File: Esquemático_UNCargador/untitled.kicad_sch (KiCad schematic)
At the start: 14 parts, among them U3.3 LM2596S-3.3, U5 LM2596S-5

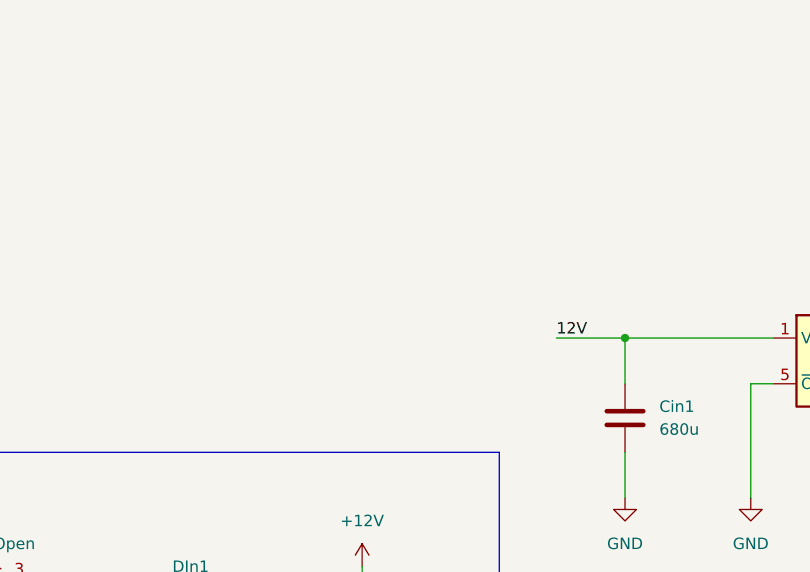
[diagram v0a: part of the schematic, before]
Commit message: Se modifica esquema del micro y se agrega página de sensores
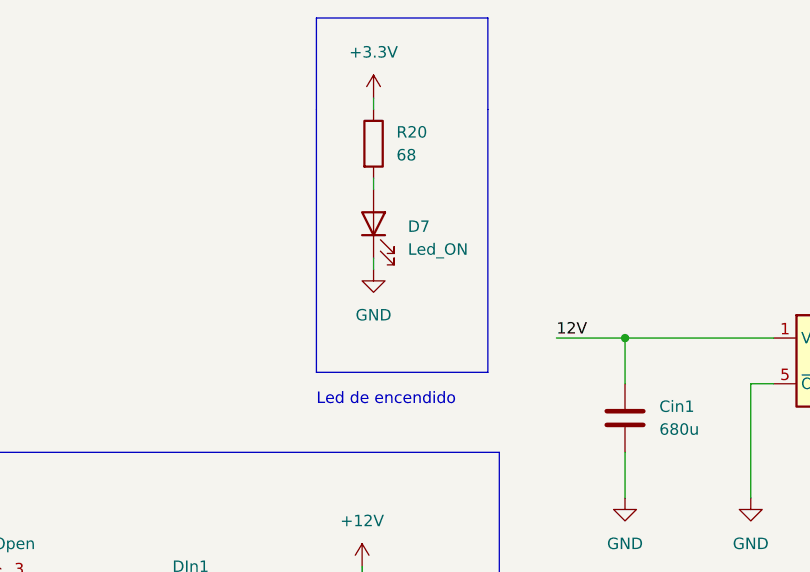
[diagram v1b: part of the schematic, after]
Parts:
- added D7: Led_ON, LED_SMD:LED_0603_1608Metric_Pad1.05x0.95mm_HandSolder, symbol LED:IR26-21C_L110_TR8
- added R20: 68, Resistor_SMD:R_1206_3216Metric_Pad1.30x1.75mm_HandSolder, symbol Device:R
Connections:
- net +3.3V: now also R20.1
- net GND: now also D7.1 (K)
- new net: D7.2 (A), R20.2
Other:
- note added: "Led de encendido"
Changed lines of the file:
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@@
+    (stroke (width 0) (type default))
+  )
+  (polyline (pts (xy 156.21 33.02) (xy 156.21 22.86))
+    (stroke (width 0) (type default))
+  )
+  (polyline (pts (xy 156.21 22.86) (xy 175.26 22.86))
+    (stroke (width 0) (type default))
+  )
+  (polyline (pts (xy 175.26 62.23) (xy 175.26 33.02))
+    (stroke (width 0) (type default))
+  )
+  (wire (pts (xy 162.56 31.75) (xy 162.56 33.02))
     (stroke (width 0) (type default))
   )
@@
     (stroke (width 0) (type default))
   )
+  (wire (pts (xy 162.56 49.53) (xy 162.56 50.8))
+    (stroke (width 0) (type default))
+  )
   (wire (pts (xy 161.29 90.17) (xy 168.91 90.17))
     (stroke (width 0) (type default))
@@
     (stroke (width 0) (type default))
   )
+  (polyline (pts (xy 156.21 33.02) (xy 156.21 62.23))
+    (stroke (width 0) (type default))
+  )
   (wire (pts (xy 219.71 120.65) (xy 219.71 128.27))
     (stroke (width 0) (type default))
@@
     (stroke (width 0) (type default))
   )
+  (wire (pts (xy 162.56 40.64) (xy 162.56 41.91))
+    (stroke (width 0) (type default))
+  )
   (wire (pts (xy 190.5 71.12) (xy 190.5 76.2))
     (stroke (width 0) (type default))
@@
   )
   (wire (pts (xy 232.41 63.5) (xy 237.49 63.5))
+    (stroke (width 0) (type default))
+  )
+  (polyline (pts (xy 175.26 22.86) (xy 175.26 33.02))
+    (stroke (width 0) (type default))
+  )
+  (polyline (pts (xy 156.21 62.23) (xy 175.26 62.23))
     (stroke (width 0) (type default))
   )
@@
     (effects (font (size 1.27 1.27)) (justify left bottom))
   )
+  (text "Led de encendido\n" (at 156.21 66.04 0)
+    (effects (font (size 1.27 1.27)) (justify left bottom))
+  )
   (label "12V" (at 182.88 110.49 0) (fields_autoplaced)
     (effects (font (size 1.27 1.27)) (justify left bottom))
@@
     )
   )
+  (symbol (lib_id "Device:R") (at 162.56 36.83 0) (unit 1)
+    (in_bom yes) (on_board yes) (dnp no) (fields_autoplaced)
+    (property "Reference" "R20" (at 165.1 35.5599 0)
+      (effects (font (size 1.27 1.27)) (justify left))
+    )
+    (property "Value" "68" (at 165.1 38.0999 0)
+      (effects (font (size 1.27 1.27)) (justify left))
+    )
+    (property "Footprint" "Resistor_SMD:R_1206_3216Metric_Pad1.30x1.75mm_HandSolder" (at 160.782 36.83 90)
+      (effects (font (size 1.27 1.27)) hide)
+    )
+    (property "Datasheet" "~" (at 162.56 36.83 0)
+      (effects (font (size 1.27 1.27)) hide)
+    )
+    (pin "1")
+    (pin "2")
+    (instances
+      (project "CircuitoPotencia"
+        (path "/f64e4c48-29c2-4644-b6e3-d55b9152fc29/c38372d7-094a-4ec0-82ac-c3a161d378bf"
+          (reference "R20") (unit 1)
+        )
+      )
+    )
+  )
   (symbol (lib_id "power:GND") (at 259.08 128.27 0) (unit 1)
     (in_bom yes) (on_board yes) (dnp no) (fields_autoplaced)
@@
         (path "/f64e4c48-29c2-4644-b6e3-d55b9152fc29/c38372d7-094a-4ec0-82ac-c3a161d378bf"
           (reference "COut1") (unit 1)
+        )
+      )
+    )
+  )
+  (symbol (lib_id "power:GND") (at 162.56 50.8 0) (unit 1)
+    (in_bom yes) (on_board yes) (dnp no) (fields_autoplaced)
+    (property "Reference" "#PWR032" (at 162.56 57.15 0)
+      (effects (font (size 1.27 1.27)) hide)
+    )
+    (property "Value" "GND" (at 162.56 55.88 0)
+      (effects (font (size 1.27 1.27)))
+    )
+    (property "Footprint" "" (at 162.56 50.8 0)
+      (effects (font (size 1.27 1.27)) hide)
+    )
+    (property "Datasheet" "" (at 162.56 50.8 0)
+      (effects (font (size 1.27 1.27)) hide)
+    )
+    (pin "1")
+    (instances
+      (project "CircuitoPotencia"
+        (path "/f64e4c48-29c2-4644-b6e3-d55b9152fc29/c38372d7-094a-4ec0-82ac-c3a161d378bf"
+          (reference "#PWR032") (unit 1)
         )
       )
@@
     )
   )
+  (symbol (lib_id "LED:IR26-21C_L110_TR8") (at 162.56 45.72 90) (unit 1)
+    (in_bom yes) (on_board yes) (dnp no) (fields_autoplaced)
+    (property "Reference" "D7" (at 166.37 46.0374 90)
+      (effects (font (size 1.27 1.27)) (justify right))
+    )
+    (property "Value" "Led_ON" (at 166.37 48.5774 90)
+      (effects (font (size 1.27 1.27)) (justify right))
+    )
+    (property "Footprint" "LED_SMD:LED_0603_1608Metric_Pad1.05x0.95mm_HandSolder" (at 157.48 45.72 0)
+      (effects (font (size 1.27 1.27)) hide)
+    )
+    (property "Datasheet" "http://www.everlight.com/file/ProductFile/IR26-21C-L110-TR8.pdf" (at 162.56 45.72 0)
+      (effects (font (size 1.27 1.27)) hide)
+    )
+    (pin "1")
+    (pin "2")
+    (instances
+      (project "CircuitoPotencia"
+        (path "/f64e4c48-29c2-4644-b6e3-d55b9152fc29/c38372d7-094a-4ec0-82ac-c3a161d378bf"
+          (reference "D7") (unit 1)
+        )
+      )
+    )
+  )
   (symbol (lib_id "power:GND") (at 161.29 109.22 0) (unit 1)
     (in_bom yes) (on_board yes) (dnp no) (fields_autoplaced)
@@
         )
       )
+    )
+  )
+  (symbol (lib_id "power:+3.3V") (at 162.56 31.75 0) (unit 1)
+    (in_bom yes) (on_board yes) (dnp no) (fields_autoplaced)
+    (property "Reference" "#PWR031" (at 162.56 35.56 0)
+      (effects (font (size 1.27 1.27)) hide)
+    )
+    (property "Value" "+3.3V" (at 162.56 26.67 0)
+      (effects (font (size 1.27 1.27)))
+    )
+    (property "Footprint" "" (at 162.56 31.75 0)
+      (effects (font (size 1.27 1.27)) hide)
+    )
+    (property "Datasheet" "" (at 162.56 31.75 0)
+      (effects (font (size 1.27 1.27)) hide)
+    )
+    (pin "1")
+    (instances
+      (project "CircuitoPotencia"
+        (path "/f64e4c48-29c2-4644-b6e3-d55b9152fc29/c38372d7-094a-4ec0-82ac-c3a161d378bf"
+          (reference "#PWR031") (unit 1)
+        )
+      )

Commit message: Pinout sensores
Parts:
- removed D7: Led_ON, LED_SMD:LED_0603_1608Metric_Pad1.05x0.95mm_HandSolder, symbol LED:IR26-21C_L110_TR8
- removed PS7: HLK-PM01, Convertidor_AC-DC:AC-DC_Converter, symbol Converter_ACDC:HLK-PM01
- removed R20: 68, Resistor_SMD:R_1206_3216Metric_Pad1.30x1.75mm_HandSolder, symbol Device:R
- added CIn? (x2): ~, symbol Device:C
- added U?: ~, symbol Regulator_Linear:LM7912_TO220
- CIn0: value 22uF -> ~; footprint Capacitor_SMD:C_0805_2012Metric_Pad1.18x1.45mm_HandSolder -> (none)
- CIn2: value 680u -> ~; footprint Capacitor_SMD:C_0201_0603Metric -> (none)
- COut1, COut2: value 220u -> ~; footprint Capacitor_SMD:C_0201_0603Metric -> (none)
- Cin1: value 680u -> ~; footprint Capacitor_SMD:C_0805_2012Metric_Pad1.18x1.45mm_HandSolder -> (none)
- D1, D2: value 1N5822 -> ~; footprint Diode_THT:D_DO-201AD_P15.24mm_Horizontal -> (none)
- DIn: renamed from DIn1; value 1N4007 -> ~; footprint Diode_SMD:D_SMA_Handsoldering -> (none)
- JP?: renamed from JP2; value Jumper_3_Open -> ~; footprint Connector_PinHeader_2.54mm:PinHeader_1x03_P2.54mm_Vertical -> (none)
- L1, L2: value 33u -> ~; footprint Inductor_SMD:L_Coilcraft_XxL4040 -> (none)
- U3.3: value LM2596S-3.3 -> ~; footprint Package_TO_SOT_SMD:TO-263-5_TabPin3 -> (none)
- U5: value LM2596S-5 -> ~; footprint Package_TO_SOT_SMD:TO-263-5_TabPin3 -> (none)
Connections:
- net GND: now also CIn?.1, CIn?.1, U?.1 (GND)
- new net: CIn?.2, U?.3 (VO)
- new net: CIn?.2, U?.2 (VI)
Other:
- note removed: "Led de encendido"
- moved on the sheet: CIn0, CIn2, COut1, COut2, Cin1, D1, D2, DIn, JP?, L1, L2, U3.3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

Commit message: Actualización11/04/2023
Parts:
- added PS1: BAC05S05DC, ConvertidorAc-DC-Footprint-Loca:AC-DC_ConverterEditado, symbol Converter_ACDC:BAC05S05DC
- CIn2, Cin1: value ~ -> 680u
- COut1, COut2: value ~ -> 220u
- L1, L2: value ~ -> 33u
- gave numbers to parts that had none: 1
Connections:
- net GND: now also PS1.4 (-Vo)
- net at JP1.2 (C): now also PS1.5 (+Vo)
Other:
- moved on the sheet: CIn0, CIn2, CIn?, COut1, COut2, Cin1, D1, D2, DIn, JP1, L1, L2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

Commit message: Actualización_huellas_Potencia
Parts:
- CIn0: value ~ -> 22mF; footprint (none) -> Capacitor_SMD:C_0805_2012Metric_Pad1.18x1.45mm_HandSolder
- DIn: value ~ -> 1N4007; footprint (none) -> Diode_SMD:D_SMA_Handsoldering
- JP1: value ~ -> Jumper; footprint (none) -> Connector_PinHeader_2.54mm:PinHeader_1x03_P2.54mm_Vertical
- L1: footprint (none) -> Inductor_SMD:L_12x12mm_H4.5mm
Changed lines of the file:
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@@
       (effects (font (size 1.27 1.27)))
     )
-    (property "Footprint" "" (at 251.46 53.34 0)
+    (property "Footprint" "Inductor_SMD:L_12x12mm_H4.5mm" (at 251.46 53.34 0)
       (effects (font (size 1.27 1.27)) hide)
     )
@@
       (effects (font (size 1.27 1.27)) (justify left))
     )
-    (property "Value" "~" (at 152.4 88.2649 0)
-      (effects (font (size 1.27 1.27)) (justify left))
-    )
-    (property "Footprint" "" (at 148.59 87.63 0)
+    (property "Value" "22mF" (at 152.4 88.2649 0)
+      (effects (font (size 1.27 1.27)) (justify left))
+    )
+    (property "Footprint" "Capacitor_SMD:C_0805_2012Metric_Pad1.18x1.45mm_HandSolder" (at 148.59 87.63 0)
       (effects (font (size 1.27 1.27)) hide)
     )
@@
       (effects (font (size 1.27 1.27)))
     )
-    (property "Value" "~" (at 129.54 74.93 0)
-      (effects (font (size 1.27 1.27)))
-    )
-    (property "Footprint" "" (at 129.54 74.295 0)
+    (property "Value" "1N4007" (at 129.54 74.93 0)
+      (effects (font (size 1.27 1.27)))
+    )
+    (property "Footprint" "Diode_SMD:D_SMA_Handsoldering" (at 129.54 74.295 0)
       (effects (font (size 1.27 1.27)) hide)
     )
@@
       (effects (font (size 1.27 1.27)))
     )
-    (property "Value" "~" (at 105.41 69.85 0)
-      (effects (font (size 1.27 1.27)))
-    )
-    (property "Footprint" "" (at 105.41 73.66 0)
-      (effects (font (size 1.27 1.27)) hide)
-    )
+    (property "Value" "Jumper" (at 105.41 69.85 0)
+      (effects (font (size 1.27 1.27)))
+    )
+    (property "Footprint" "Connector_PinHeader_2.54mm:PinHeader_1x03_P2.54mm_Vertical" (at 105.41 73.66 0)
+      (effects (font (size 1.27 1.27)) hide)
+    )

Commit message: Huella_Induct
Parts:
- CIn0: value 22mF -> 22uF
- COut1, COut2: footprint (none) -> Capacitor_SMD:CP_Elec_8x10
- L1: footprint Inductor_SMD:L_12x12mm_H4.5mm -> Inductor_SMD:L_12x12mm_H8mm
- L2: footprint (none) -> Inductor_SMD:L_12x12mm_H8mm

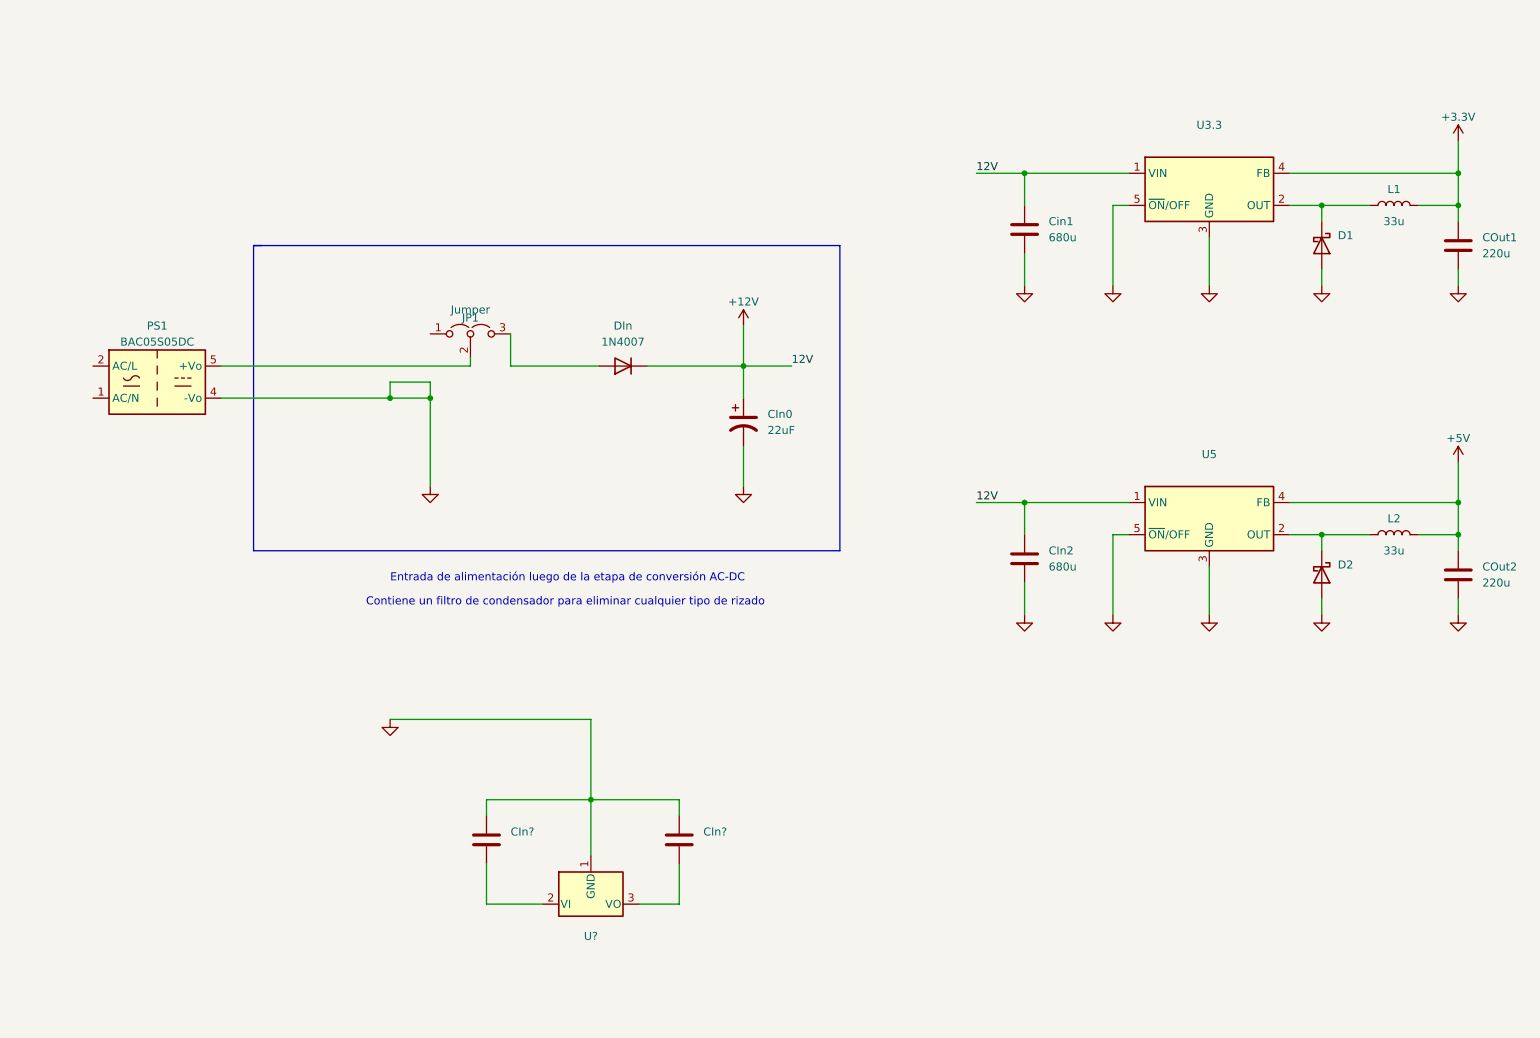
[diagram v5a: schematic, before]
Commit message: Avances en Huellas
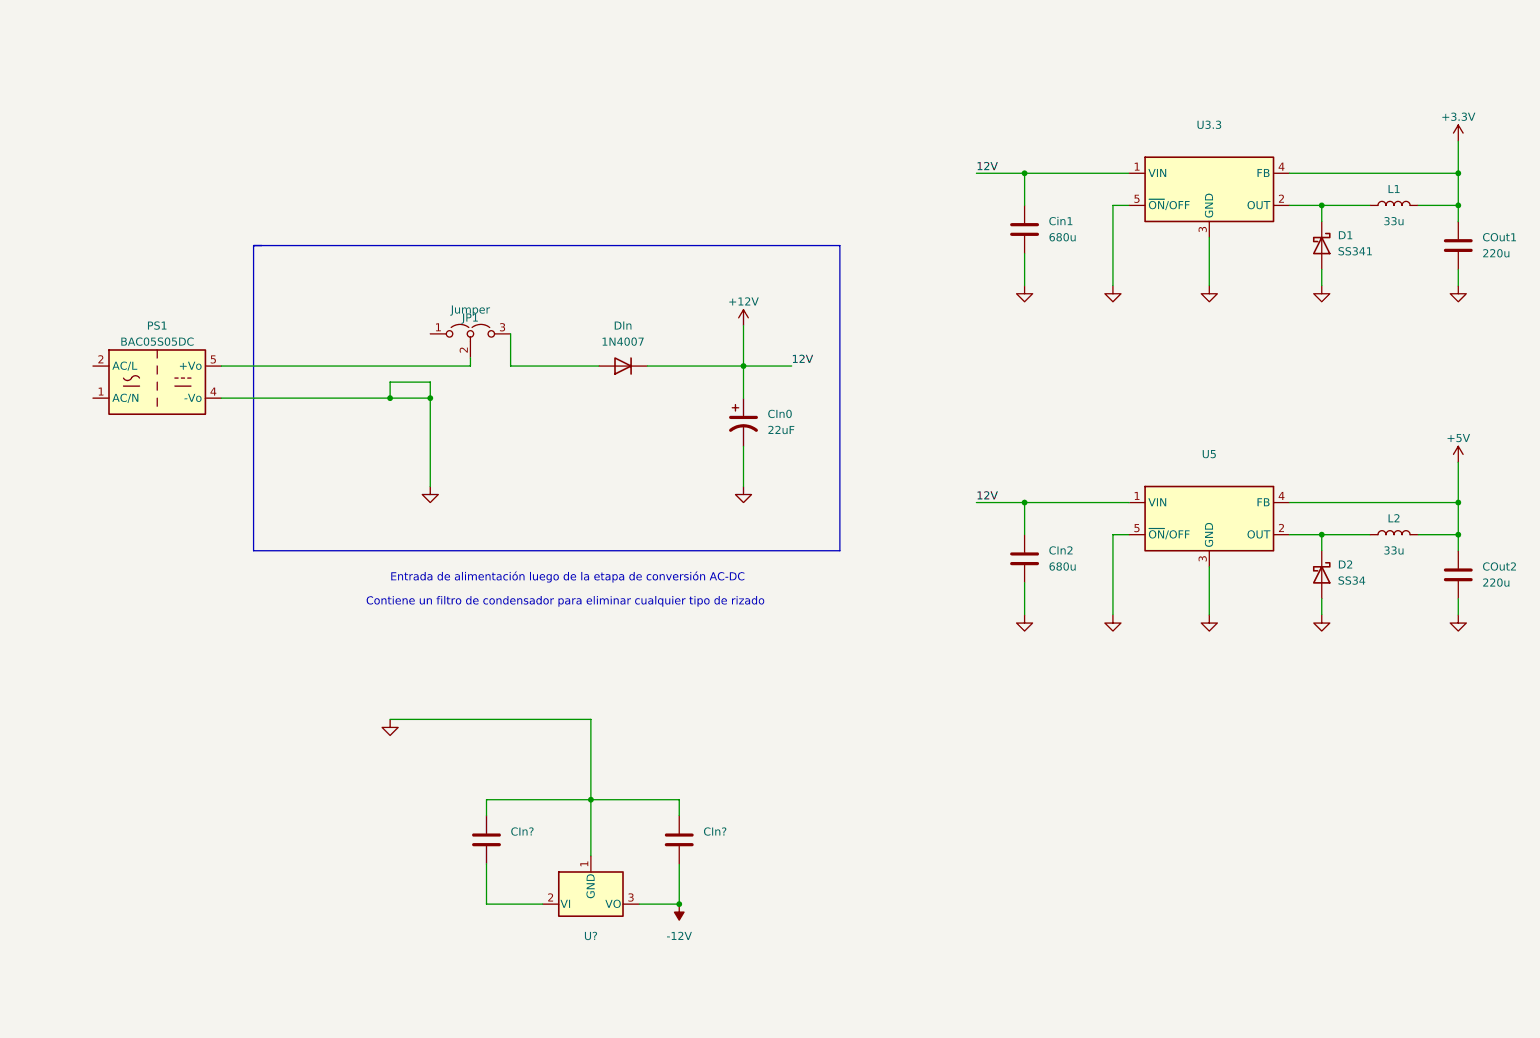
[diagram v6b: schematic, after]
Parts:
- CIn2, CIn? (x2), Cin1: footprint (none) -> Capacitor_THT:C_Radial_D10.0mm_H16.0mm_P5.00mm
- D1: value ~ -> SS341; footprint (none) -> Diode_SMD:D_SMA_Handsoldering
- D2: value ~ -> SS34; footprint (none) -> Diode_SMD:D_SMA_Handsoldering
- PS1: footprint ConvertidorAc-DC-Footprint-Loca:AC-DC_ConverterEditado -> Convertidor_AC-DC:AC-DC_Converter
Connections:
- net -12V: now reaches CIn?.2, U?.3 (VO)
